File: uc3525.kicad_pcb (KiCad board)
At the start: 2 copper layers, 72.9 x 57.2 mm, 28 parts, among them J1 IN, J2 Amostra, J3 OUT, Q1 PN2222A, Q2 2N2907A, U1 UC3525

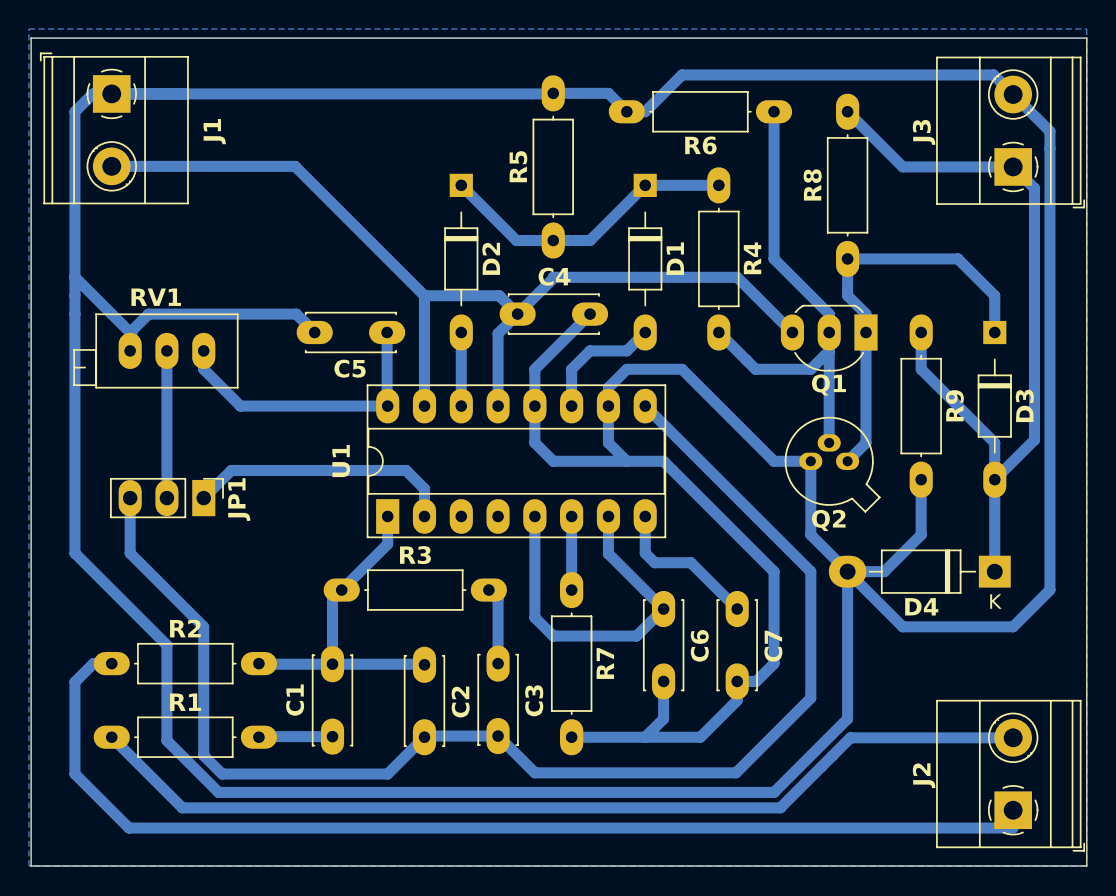
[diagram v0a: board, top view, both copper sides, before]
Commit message: Aumento da distância entre as trilhas.
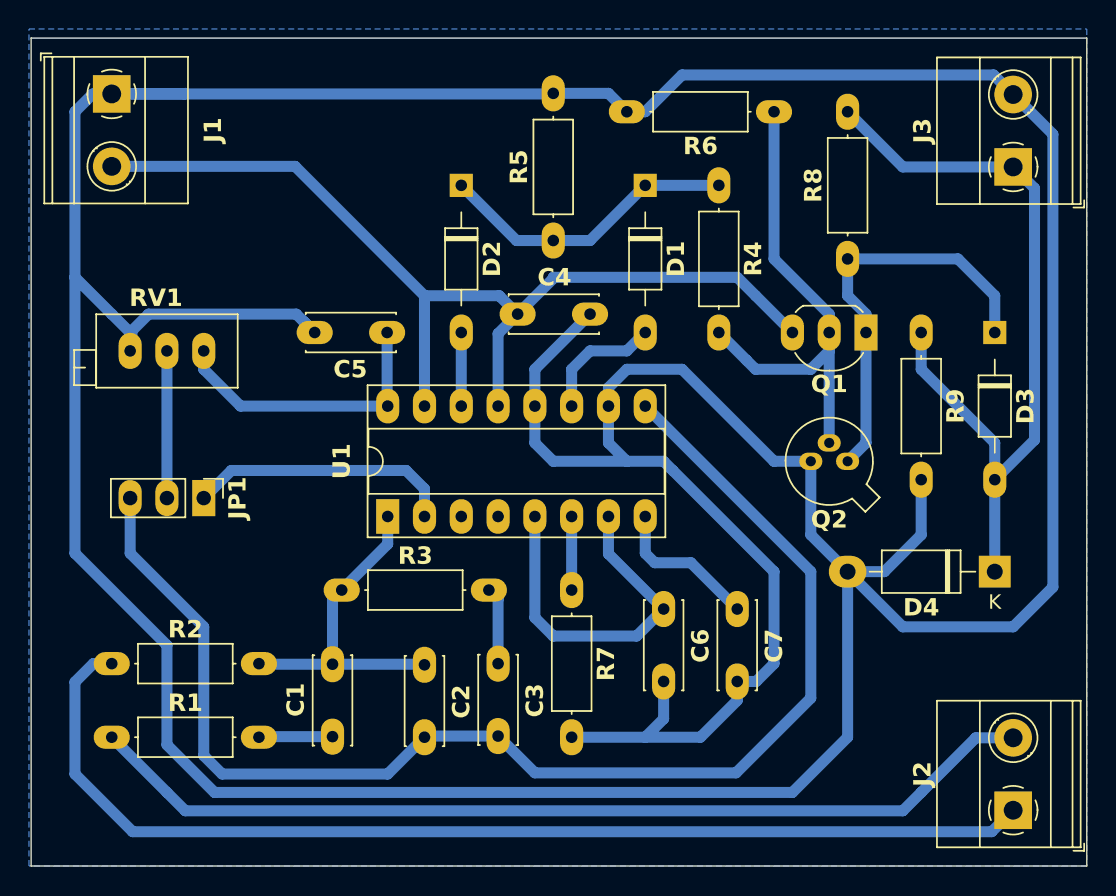
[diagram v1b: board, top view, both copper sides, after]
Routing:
- net GND: track 353.9 -> 354.9 mm
- net Net-(J2-Pin_1): track 75.7 -> 76.4 mm
